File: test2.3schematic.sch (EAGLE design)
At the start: 27 parts, among them IC1 FXLN8371QR1, IC2 OPA4990IDR, IC3 ICL7660CSA+, IC4 MAX25210ATAB9_V+, J1 2-1445057-5

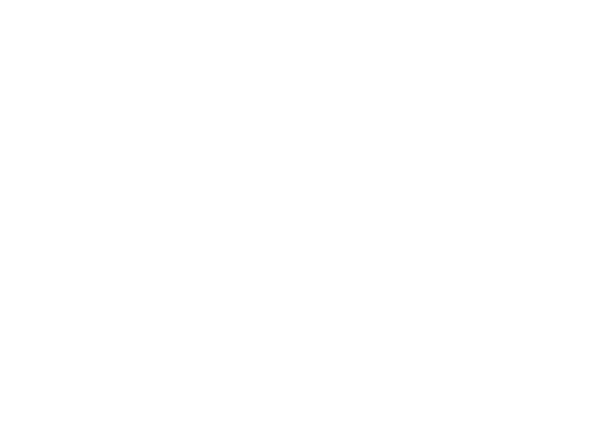
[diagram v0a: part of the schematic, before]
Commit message: Adding random Connector for testing
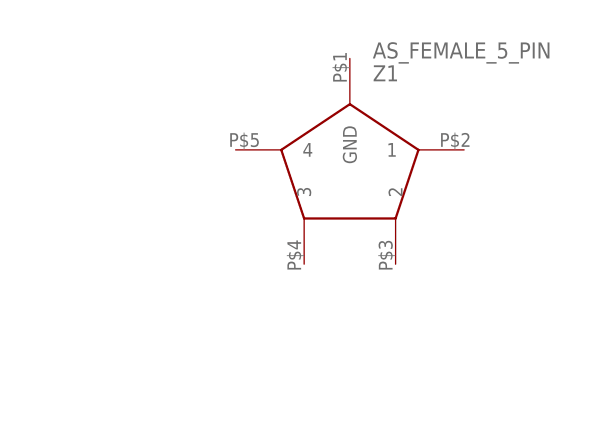
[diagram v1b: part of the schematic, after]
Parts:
- added Z1: AS_FEMALE_5_PIN, SamacSys_Parts:AS_FEMALE_5_PIN
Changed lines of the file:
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@@
 <part name="J1" library="SamacSys_Parts" deviceset="2-1445057-5" device=""/>
 <part name="R1_10K" library="SamacSys_Parts" deviceset="CRCW020110K0FNED" device=""/>
+<part name="Z1" library="SamacSys_Parts" deviceset="AS_FEMALE_5_PIN" device=""/>
 </parts>
 <sheets>
@@
 <attribute name="NAME" x="52.07" y="-39.37" size="1.778" layer="95" rot="R270" align="center-left"/>
 <attribute name="VALUE" x="49.53" y="-39.37" size="1.778" layer="96" rot="R270" align="center-left"/>
+</instance>
+<instance part="Z1" gate="Z$1" x="182.88" y="91.44" smashed="yes">
+<attribute name="VALUE" x="185.42" y="104.14" size="1.778" layer="96"/>
+<attribute name="NAME" x="185.42" y="101.6" size="1.778" layer="95"/>
 </instance>
 </instances>
@@
 packages will not be understood (or retained) with this version.
 </note>
+<note version="8.5" severity="warning">
+Since Version 8.5, EAGLE supports locking for holes, vias, wires and polygons.
+The locking property on all objects of these types will not be understood in this version.
+</note>
 </compatibility>

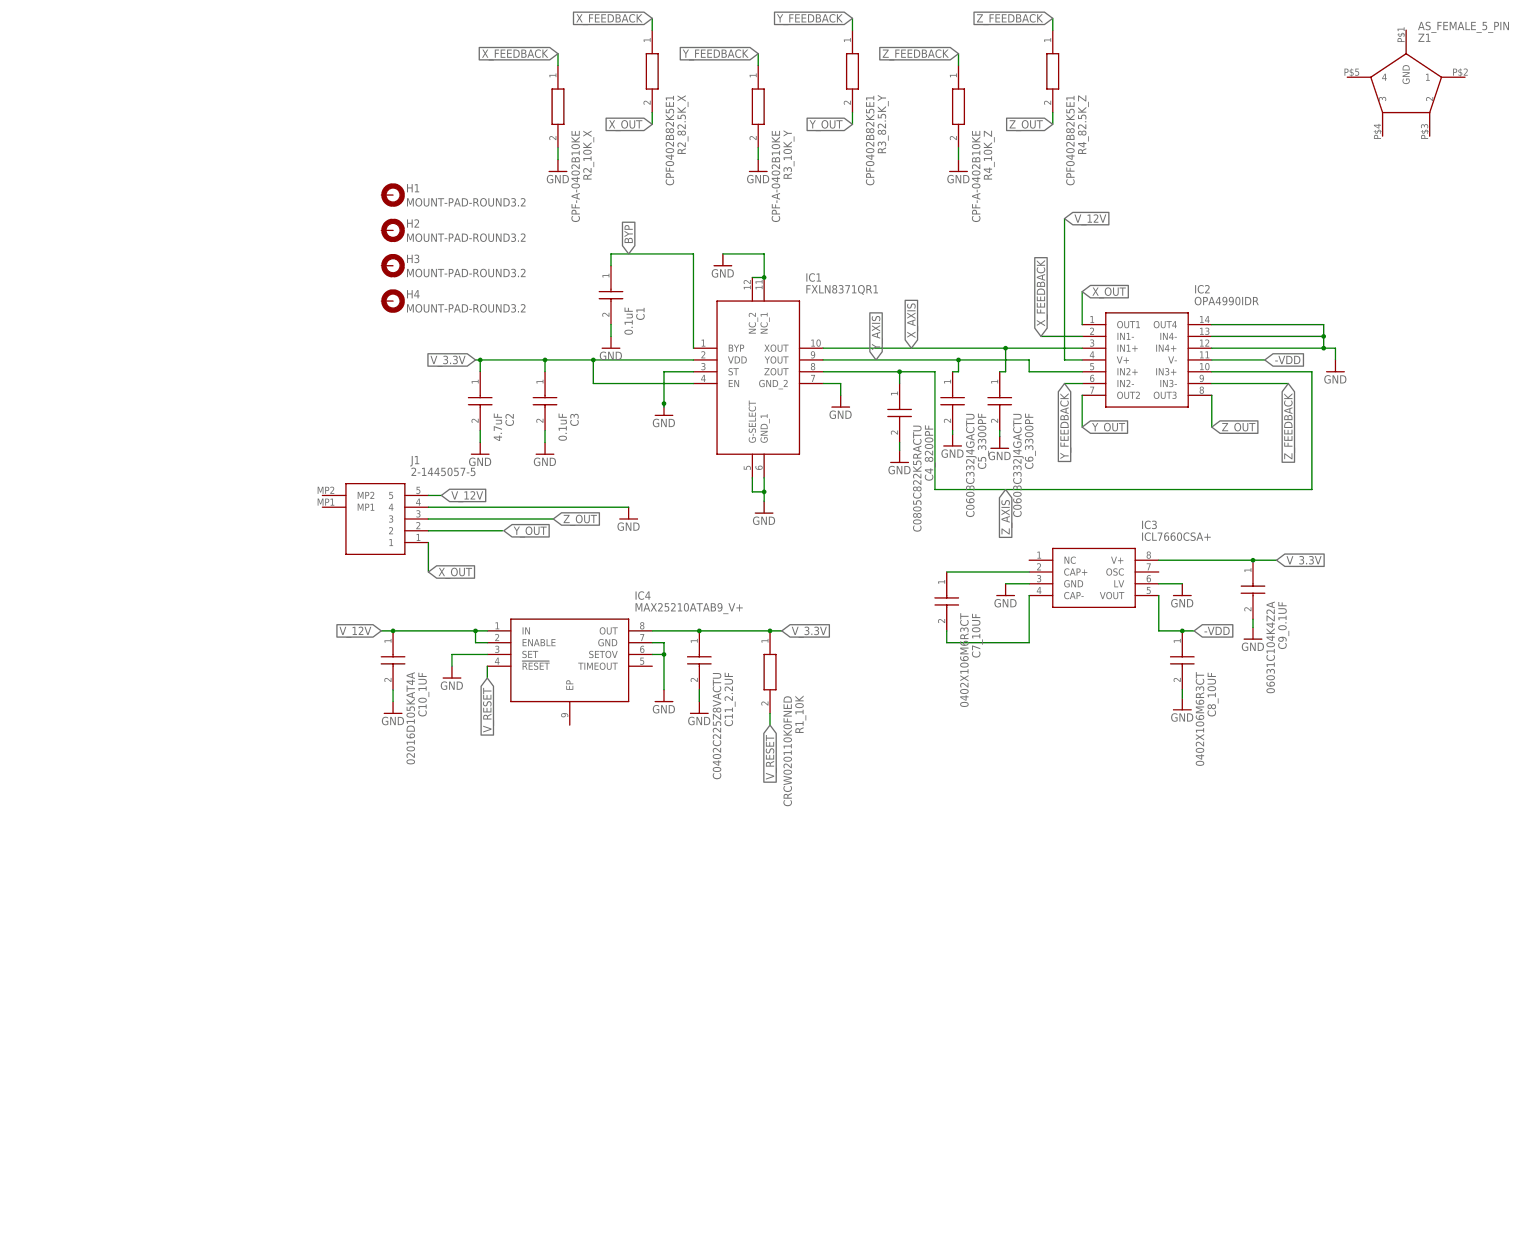
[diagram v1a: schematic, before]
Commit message: Schematics done and capacitors have 3d packages
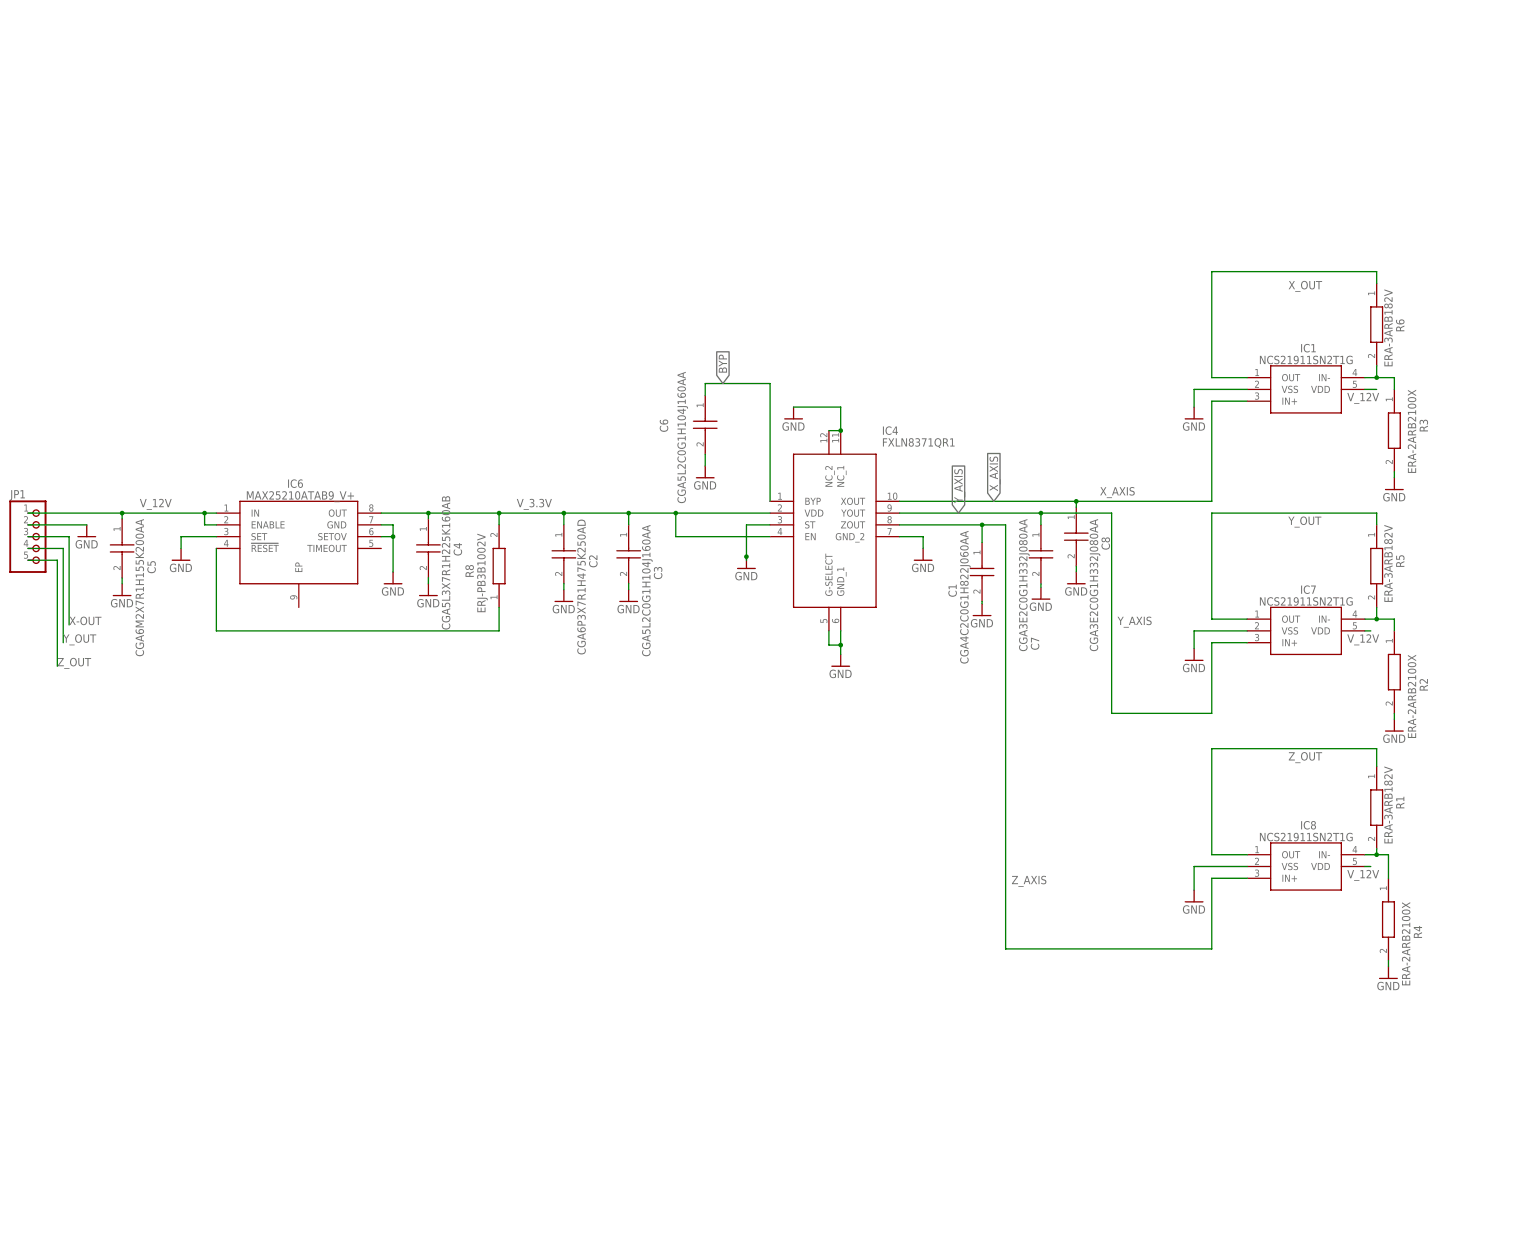
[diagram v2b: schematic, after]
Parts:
- removed C10_1UF: 02016D105KAT4A, SamacSys_Parts:02016D105KAT4A
- removed C11_2.2UF: C0402C225Z8VACTU, SamacSys_Parts:C0402C225Z8VACTU
- removed C4_8200PF: C0805C822K5RACTU, SamacSys_Parts:C0805C822K5RACTU
- removed C5_3300PF, C6_3300PF: C0603C332J4GACTU, SamacSys_Parts:C0603C332J4GACTU
- removed C7_10UF, C8_10UF: 0402X106M6R3CT, SamacSys_Parts:0402X106M6R3CT
- removed C9_0.1UF: 06031C104K4Z2A, SamacSys_Parts:06031C104K4Z2A
- removed H1, H2, H3, H4: MOUNT-PAD-ROUND3.2, holes:MOUNT-PAD-ROUND3.2
- removed IC2: OPA4990IDR, SamacSys_Parts:OPA4990IDR
- removed IC3: ICL7660CSA+, SamacSys_Parts:ICL7660CSA+
- removed J1: 2-1445057-5, SamacSys_Parts:2-1445057-5
- removed R1_10K: CRCW020110K0FNED, SamacSys_Parts:CRCW020110K0FNED
- removed R2_10K_X, R3_10K_Y, R4_10K_Z: CPF-A-0402B10KE, SamacSys_Parts:CPF-A-0402B10KE
- removed R2_82.5K_X, R3_82.5K_Y, R4_82.5K_Z: CPF0402B82K5E1, SamacSys_Parts:CPF0402B82K5E1
- removed Z1: AS_FEMALE_5_PIN, SamacSys_Parts:AS_FEMALE_5_PIN
- added C4: CGA5L3X7R1H225K160AB, SamacSys_Parts:CGA5L3X7R1H225K160AB
- added C5: CGA6M2X7R1H155K200AA, SamacSys_Parts:CGA6M2X7R1H155K200AA
- added C6: CGA5L2C0G1H104J160AA, SamacSys_Parts:CGA5L2C0G1H104J160AA
- added C7, C8: CGA3E2C0G1H332J080AA, SamacSys_Parts:CGA3E2C0G1H332J080AA
- added IC6: MAX25210ATAB9_V+, SamacSys_Parts:MAX25210ATAB9_V+
- added IC7, IC8: NCS21911SN2T1G, SamacSys_Parts:NCS21911SN2T1G
- added JP1: (no value), pinhead:PINHD-1X5
- added R1, R5, R6: ERA-3ARB182V, SamacSys_Parts:ERA-3ARB182V
- added R2, R3, R4: ERA-2ARB2100X, SamacSys_Parts:ERA-2ARB2100X
- added R8: ERJ-PB3B1002V, SamacSys_Parts:ERJ-PB3B1002V
- C1: value 0.1uF -> CGA4C2C0G1H822J060AA; device SamacSys_Parts:06031C104K4Z2A -> SamacSys_Parts:CGA4C2C0G1H822J060AA
- C2: value 4.7uF -> CGA6P3X7R1H475K250AD; device SamacSys_Parts:CL21A475KPFNNNG -> SamacSys_Parts:CGA6P3X7R1H475K250AD
- C3: value 0.1uF -> CGA5L2C0G1H104J160AA; device SamacSys_Parts:06031C104K4Z2A -> SamacSys_Parts:CGA5L2C0G1H104J160AA
- IC1: value FXLN8371QR1 -> NCS21911SN2T1G; device SamacSys_Parts:FXLN8371QR1 -> SamacSys_Parts:NCS21911SN2T1G
- IC4: value MAX25210ATAB9_V+ -> FXLN8371QR1; device SamacSys_Parts:MAX25210ATAB9_V+ -> SamacSys_Parts:FXLN8371QR1
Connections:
- removed net -VDD: C8_10UF.1, IC2.V-, IC3.VOUT
- removed net N$1: C7_10UF.1, IC3.CAP+
- removed net N$2: C7_10UF.2, IC3.CAP-
- removed net X_FEEDBACK: IC2.IN1-, R2_10K_X.1, R2_82.5K_X.1
- removed net Y_FEEDBACK: IC2.IN2-, R3_10K_Y.1, R3_82.5K_Y.1
- removed net Z_FEEDBACK: IC2.IN3-, R4_10K_Z.1, R4_82.5K_Z.1
- new net X-OUT: JP1.3
- net BYP: now also C6.1, IC4.BYP; no longer C1.1, IC1.BYP
- net GND: now also C4.2, C5.2, C6.2, C7.2, C8.2, IC1.VSS, IC4.G-SELECT, IC4.GND_1, IC4.GND_2, IC4.NC_1, IC4.NC_2, IC4.ST, IC6.GND, IC6.SET, IC6.SETOV, IC7.VSS, IC8.VSS, JP1.2, R2.2, R3.2, R4.2; no longer C10_1UF.2, C11_2.2UF.2, C4_8200PF.2, C5_3300PF.2, C6_3300PF.2, C8_10UF.2, C9_0.1UF.2, IC1.G-SELECT, IC1.GND_1, IC1.GND_2, IC1.NC_1, IC1.NC_2, IC1.ST, IC2.IN4+, IC2.IN4-, IC2.OUT4, IC3.GND, IC3.LV, IC4.GND, IC4.SET, IC4.SETOV, J1.4, R2_10K_X.2, R3_10K_Y.2, R4_10K_Z.2
- net V_12V: now also C5.1, IC1.VDD, IC6.ENABLE, IC6.IN, IC7.VDD, IC8.VDD, JP1.1; no longer C10_1UF.1, IC2.V+, IC4.ENABLE, IC4.IN, J1.5
- net V_3.3V: now also C4.1, IC4.EN, IC4.VDD, IC6.OUT, R8.2; no longer C11_2.2UF.1, C9_0.1UF.1, IC1.EN, IC1.VDD, IC3.V+, IC4.OUT, R1_10K.1
- net V_RESET: now also IC6.!RESET, R8.1; no longer IC4.!RESET, R1_10K.2
- net X_AXIS: now also C8.1, IC1.IN+, IC4.XOUT; no longer C6_3300PF.1, IC1.XOUT, IC2.IN1+
- net X_OUT: now also IC1.IN-, IC1.OUT, R3.1, R6.1, R6.2; no longer IC2.OUT1, J1.1, R2_82.5K_X.2
- net Y_AXIS: now also C7.1, IC4.YOUT, IC7.IN+; no longer C5_3300PF.1, IC1.YOUT, IC2.IN2+
- net Y_OUT: now also IC7.IN-, IC7.OUT, JP1.4, R2.1, R5.1, R5.2; no longer IC2.OUT2, J1.2, R3_82.5K_Y.2
- net Z_AXIS: now also C1.1, IC4.ZOUT, IC8.IN+; no longer C4_8200PF.1, IC1.ZOUT, IC2.IN3+
- net Z_OUT: now also IC8.IN-, IC8.OUT, JP1.5, R1.1, R1.2, R4.1; no longer IC2.OUT3, J1.3, R4_82.5K_Z.2
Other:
- moved on the sheet: C1, C2, C3

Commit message: All 3d parts added and Decoupling capacitorss placed on Op amps volatges
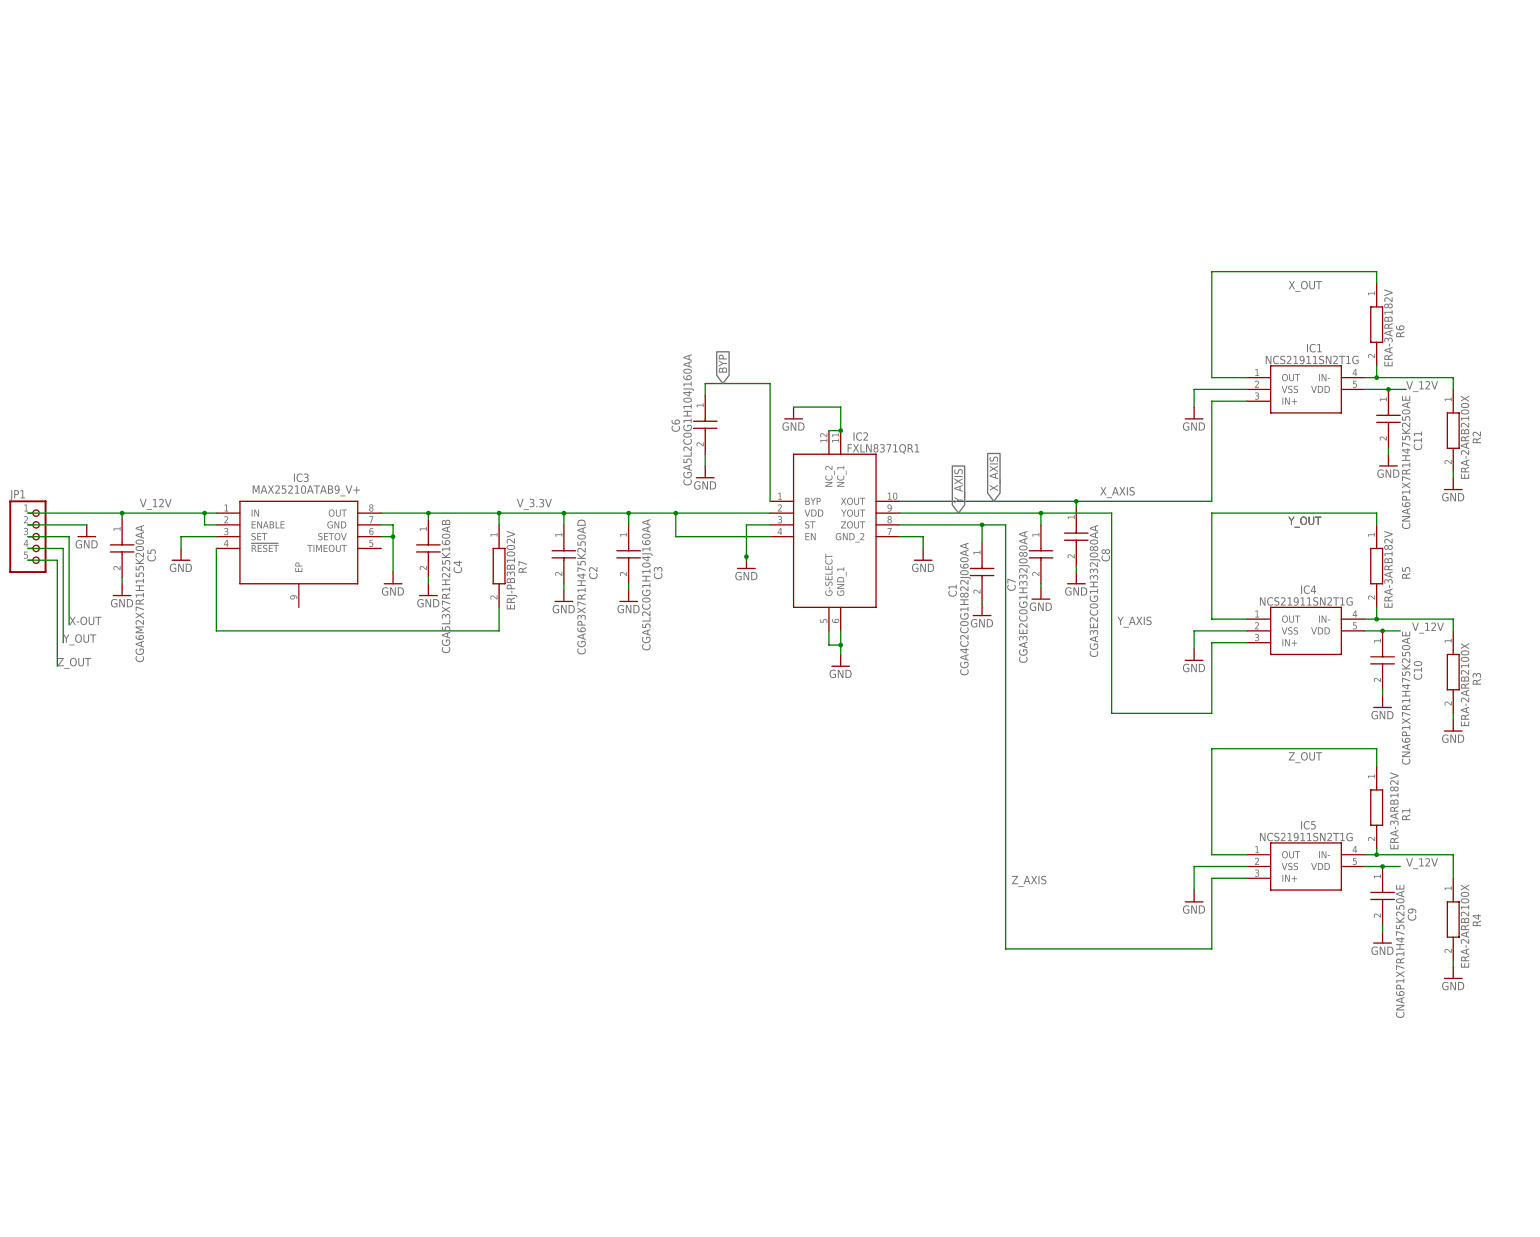
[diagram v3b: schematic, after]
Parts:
- removed IC7: NCS21911SN2T1G, SamacSys_Parts:NCS21911SN2T1G
- removed R8: ERJ-PB3B1002V, SamacSys_Parts:ERJ-PB3B1002V
- added C10, C11, C9: CNA6P1X7R1H475K250AE, SamacSys_Parts:CNA6P1X7R1H475K250AE
- added IC2: FXLN8371QR1, SamacSys_Parts:FXLN8371QR1
- added R7: ERJ-PB3B1002V, SamacSys_Parts:ERJ-PB3B1002V
- IC4: value FXLN8371QR1 -> NCS21911SN2T1G; device SamacSys_Parts:FXLN8371QR1 -> SamacSys_Parts:NCS21911SN2T1G
- renumbered IC6 to IC3, IC8 to IC5
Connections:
- net BYP: now also IC2.BYP; no longer IC4.BYP
- net GND: now also C10.2, C11.2, C9.2, IC2.G-SELECT, IC2.GND_1, IC2.GND_2, IC2.NC_1, IC2.NC_2, IC2.ST, IC4.VSS; no longer IC4.G-SELECT, IC4.GND_1, IC4.GND_2, IC4.NC_1, IC4.NC_2, IC4.ST, IC7.VSS
- net V_12V: now also C10.1, C11.1, C9.1, IC4.VDD; no longer IC7.VDD
- net V_3.3V: now also IC2.EN, IC2.VDD, R7.1; no longer IC4.EN, IC4.VDD, R8.2
- net V_RESET: now also R7.2; no longer R8.1
- net X_AXIS: now also IC2.XOUT; no longer IC4.XOUT
- net X_OUT: now also R2.1; no longer R3.1
- net Y_AXIS: now also IC2.YOUT, IC4.IN+; no longer IC4.YOUT, IC7.IN+
- net Y_OUT: now also IC4.IN-, IC4.OUT, R3.1; no longer IC7.IN-, IC7.OUT, R2.1
- net Z_AXIS: now also IC2.ZOUT; no longer IC4.ZOUT
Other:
- moved on the sheet: R2, R3, R4
